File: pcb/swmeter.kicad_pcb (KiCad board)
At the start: 2 copper layers, 53 x 66 mm, 30 parts, among them J0 Conn_01x02_Female, J1 AudioPlug, J2 Conn_Coaxial, J3 Conn_01x03_Female, J4 Conn_01x03_Female, SW1 SW_SPDT, SW2 SW_SPDT, SW3 SW_DIP_x03, U1 LM3914N

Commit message: optimized trimmer schematics
optimized trimmer schematics
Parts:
- added RV3: 1,2kΩ, Potentiometer_THT:Potentiometer_Bourns_3266Y_Vertical, F.Cu at (254.8, 117.5)
- J3, J4: footprint Connector_PinHeader_1.27mm:PinHeader_1x03_P1.27mm_Vertical -> Connector_PinHeader_2.54mm:PinHeader_1x03_P2.54mm_Vertical
- R1: value 1.2kΩ -> R; footprint Resistor_THT:R_Axial_DIN0207_L6.3mm_D2.5mm_P10.16mm_Horizontal -> Resistor_THT:R_Axial_DIN0207_L6.3mm_D2.5mm_P7.62mm_Horizontal
- moved R1 29.0 mm to (232.7, 131.0), turned to -90 degrees
- moved C1 4.72 mm to (228.3, 133.3)
- moved J4 2.89 mm to (259.2, 104.8)
- moved J0 2.81 mm to (220.2, 136.6)
- moved RV2 2.54 mm to (254.8, 111.2)
- moved J3 1.07 mm to (249.4, 98.8)
- moved D0 0.41 mm to (247.9, 104.7)
- moved SW2 0.17 mm to (247.9, 91.1)
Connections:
- C1 pad 1: Net-(BAR1-Pad1) -> Net-(C1-Pad1)
- J3 pad 3: Net-(BAR1-Pad1) -> Net-(C1-Pad1)
- J4 pad 1: Net-(J4-Pad1) -> GND
- R1 pad 1: Net-(J4-Pad1) -> Net-(C1-Pad1)
- R1 pad 2: Net-(J4-Pad3) -> Net-(BAR1-Pad1)
- RV2 pad 2: Net-(J4-Pad1) -> GND
- SW1 pad 3: Net-(BAR1-Pad1) -> Net-(C1-Pad1)
- SW3 pad 3: Net-(BAR1-Pad1) -> Net-(C1-Pad1)
- U1 pad 3: Net-(BAR1-Pad1) -> Net-(C1-Pad1)
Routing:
- net Net-(C1-Pad1): track 0.00 -> 94.1 mm
- net Net-(BAR1-Pad1): track 124.5 -> 31.5 mm
- net Net-(J4-Pad1): track 16.4 -> 0.00 mm
- net Net-(J4-Pad2): track 25.5 -> 38.1 mm
- net Net-(J4-Pad3): track 25.5 -> 36.6 mm
- net GND: track 0.45 -> 9.58 mm, vias 77 -> 70
- net +9V: track 5.86 -> 8.46 mm
- net Net-(D0-Pad1): track 9.34 -> 8.14 mm
- net Net-(SW3-Pad4): track 15.0 -> 15.7 mm
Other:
- outline, holes or cut-outs redrawn
- board text added: "GND/RefAdj/RHI&Fout"
- board text added: "LED-Bargraph"
- board text added: "RHI&Fout/RefAdj/GND"
- board text added: "RV3"
- board text added: "SW-Meter v0.7 © WodoWiesel 24/11/2023"
- board text removed: "LED_Bargraph"
- board text removed: "REF"
- board text removed: "RHI&Fout/RefAdj/RVar"
- board text removed: "RVar/RefAdj/RHI&Fout"
- board text removed: "SW-Meter v0.6 © WodoWiesel 15/04/2023"

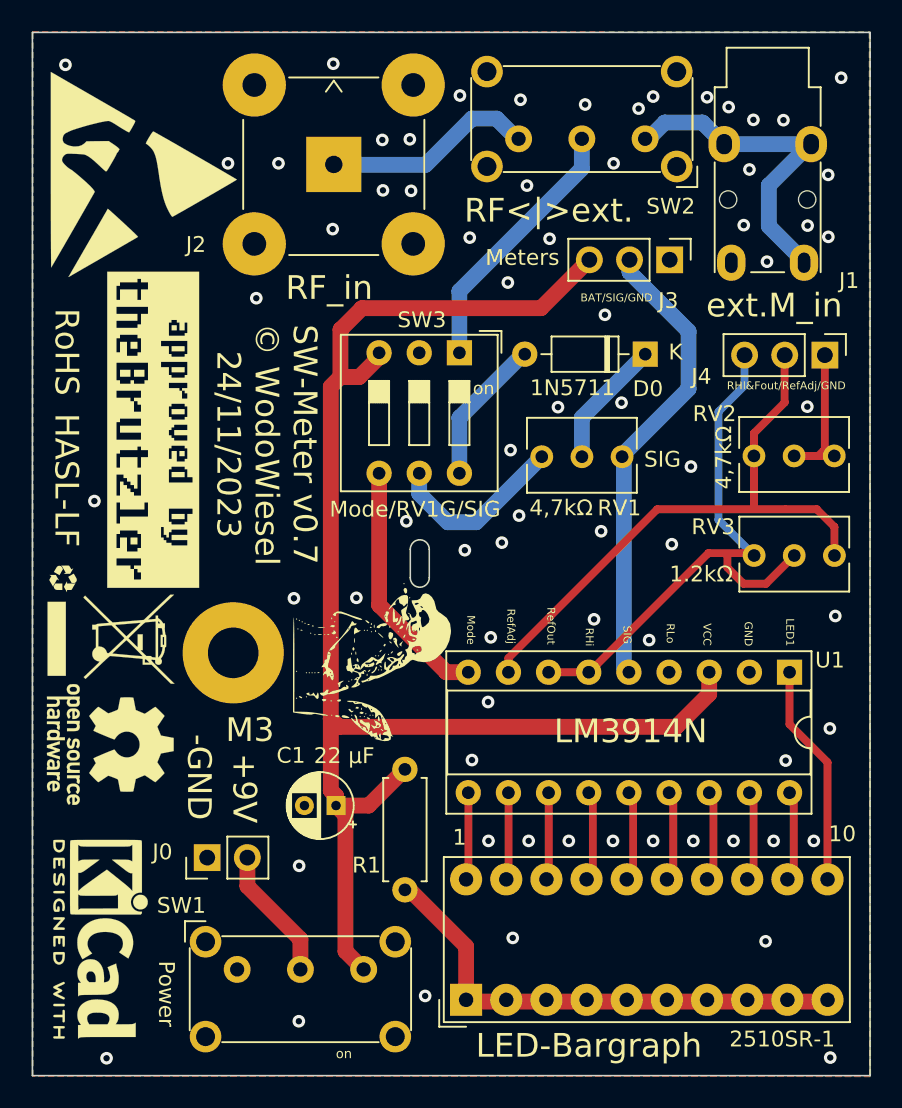
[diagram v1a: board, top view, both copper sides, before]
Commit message: add diode for reverse polarity protection
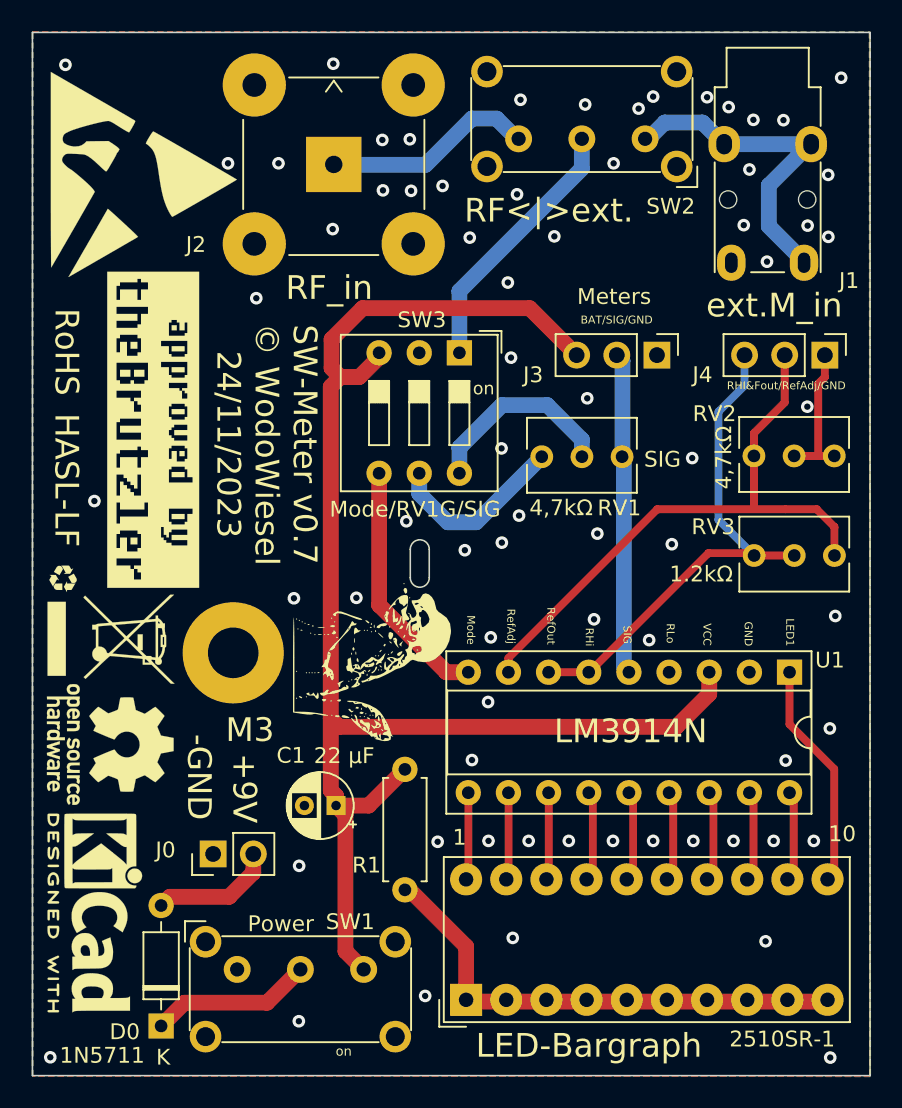
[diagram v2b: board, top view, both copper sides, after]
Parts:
- R1: value R -> 330Ω
- moved D0 52.4 mm to (217.3, 147.2), turned to 90 degrees
- moved J3 6.08 mm to (248.6, 104.8)
- moved REF8** 1.70 mm to (213.1, 140.1)
- moved REF88** 1.52 mm to (212.9, 140.2)
- moved J0 0.44 mm to (220.6, 136.3)
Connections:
- D0 pad 2: Net-(D0-Pad2) -> +9V
- RV1 pad 2: Net-(D0-Pad1) -> Net-(RV1-Pad2)
- SW1 pad 2: +9V -> Net-(D0-Pad1)
- SW3 pad 6: Net-(D0-Pad2) -> Net-(RV1-Pad2)
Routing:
- net Net-(RV1-Pad2): track 0.00 -> 12.5 mm
- net Net-(D0-Pad2): track 9.31 -> 0.00 mm
- net Net-(J3-Pad2): track 29.6 -> 20.4 mm
- net Net-(J4-Pad3): track 36.6 -> 33.0 mm
- net Net-(D0-Pad1): track 8.14 -> 10.3 mm
- net +9V: track 8.46 -> 7.87 mm
